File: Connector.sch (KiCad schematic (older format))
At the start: 1 part, among them J1 776163-1

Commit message: Added IO Lables
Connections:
- net labels added: +5VD, Accelerator_1, Accelerator_2, Brake_1, Brake_2, CAN_H, CAN_L, EmergencyStop, GND, GNDD, GearDrive, GearParking, GearReverse, HALL_1_+, HALL_1_-, HALL_2_+, HALL_2_-, HALL_3_+, HALL_3_-, HighVoltageOn, IgnitionOn, LeftSupport, NTC_AW_1, NTC_AW_2, NTC_FW_1, NTC_FW_2, ParkingBrake, PowerContactorOn, PowerSteeringPWM, ReverseLight, RightSupport, ShuntContactorOn, VIN
- net labels removed: +BATT, -BATT
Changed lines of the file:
@@
 $EndComp
 $Comp
-L power:+BATT #PWR?
-U 1 1 60F698CF
-P 3000 2400
-F 0 "#PWR?" H 3000 2250 50  0001 C CNN
-F 1 "+BATT" V 3015 2528 50  0000 L CNN
-F 2 "" H 3000 2400 50  0001 C CNN
-F 3 "" H 3000 2400 50  0001 C CNN
-	1    3000 2400
+L MyLibrary:VIN #PWR?
+U 1 1 610918C9
+P 3500 2150
+F 0 "#PWR?" H 3500 2000 50  0001 C CNN
+F 1 "VIN" V 3515 2278 50  0000 L CNN
+F 2 "" H 3500 2150 50  0001 C CNN
+F 3 "" H 3500 2150 50  0001 C CNN
+	1    3500 2150
 	0    1    1    0
 $EndComp
 $Comp
-L power:-BATT #PWR?
-U 1 1 60F6A98D
-P 3000 2550
-F 0 "#PWR?" H 3000 2400 50  0001 C CNN
-F 1 "-BATT" V 3015 2678 50  0000 L CNN
-F 2 "" H 3000 2550 50  0001 C CNN
-F 3 "" H 3000 2550 50  0001 C CNN
-	1    3000 2550
+L power:GND #PWR?
+U 1 1 61091F33
+P 3500 2250
+F 0 "#PWR?" H 3500 2000 50  0001 C CNN
+F 1 "GND" V 3505 2122 50  0000 R CNN
+F 2 "" H 3500 2250 50  0001 C CNN
+F 3 "" H 3500 2250 50  0001 C CNN
+	1    3500 2250
+	0    -1   -1   0
+$EndComp
+Text Label 3500 2500 0    50   ~ 0
+HALL_1_+
+Text Label 3500 2600 0    50   ~ 0
+HALL_1_-
+Text Label 3500 2700 0    50   ~ 0
+HALL_2_+
+Text Label 3500 2800 0    50   ~ 0
+HALL_2_-
+Text Label 3500 2900 0    50   ~ 0
+HALL_3_+
+Text Label 3500 3000 0    50   ~ 0
+HALL_3_-
+$Comp
+L power:+5VD #PWR?
+U 1 1 61093076
+P 3500 3100
+F 0 "#PWR?" H 3500 2950 50  0001 C CNN
+F 1 "+5VD" V 3515 3228 50  0000 L CNN
+F 2 "" H 3500 3100 50  0001 C CNN
+F 3 "" H 3500 3100 50  0001 C CNN
+	1    3500 3100
 	0    1    1    0
 $EndComp
+$Comp
+L power:GNDD #PWR?
+U 1 1 61093201
+P 3500 3200
+F 0 "#PWR?" H 3500 2950 50  0001 C CNN
+F 1 "GNDD" V 3504 3090 50  0000 R CNN
+F 2 "" H 3500 3200 50  0001 C CNN
+F 3 "" H 3500 3200 50  0001 C CNN
+	1    3500 3200
+	0    -1   -1   0
+$EndComp
+Text Label 3500 3350 0    50   ~ 0
+NTC_FW_1
+Text Label 3500 3450 0    50   ~ 0
+NTC_FW_2
+Text Label 3500 3550 0    50   ~ 0
+NTC_AW_1
+Text Label 3500 3650 0    50   ~ 0
+NTC_AW_2
+Text Label 3500 3850 0    50   ~ 0
+CAN_H
+Text Label 3500 3950 0    50   ~ 0
+CAN_L
+Text Label 3500 4200 0    50   ~ 0
+RightSupport
+Text Label 3500 4300 0    50   ~ 0
+LeftSupport
+Text Label 3500 4400 0    50   ~ 0
+IgnitionOn
+Text Label 3500 4500 0    50   ~ 0
+HighVoltageOn
+Text Label 3500 4600 0    50   ~ 0
+GearDrive
+Text Label 3500 4700 0    50   ~ 0
+GearReverse
+Text Label 3500 4800 0    50   ~ 0
+GearParking
+Text Label 3500 4900 0    50   ~ 0
+EmergencyStop
+Text Label 3500 5150 0    50   ~ 0
+ReverseLight
+Text Label 3500 5250 0    50   ~ 0
+ParkingBrake
+Text Label 3500 5350 0    50   ~ 0
+PowerContactorOn
+Text Label 3500 5450 0    50   ~ 0
+ShuntContactorOn
+Text Label 3500 5550 0    50   ~ 0
+PowerSteeringPWM
+Text Label 3500 5850 0    50   ~ 0
+Accelerator_1
+Text Label 3500 5950 0    50   ~ 0
+Accelerator_2
+Text Label 3500 6050 0    50   ~ 0
+Brake_1
+Text Label 3500 6150 0    50   ~ 0
+Brake_2
 $EndSCHEMATC

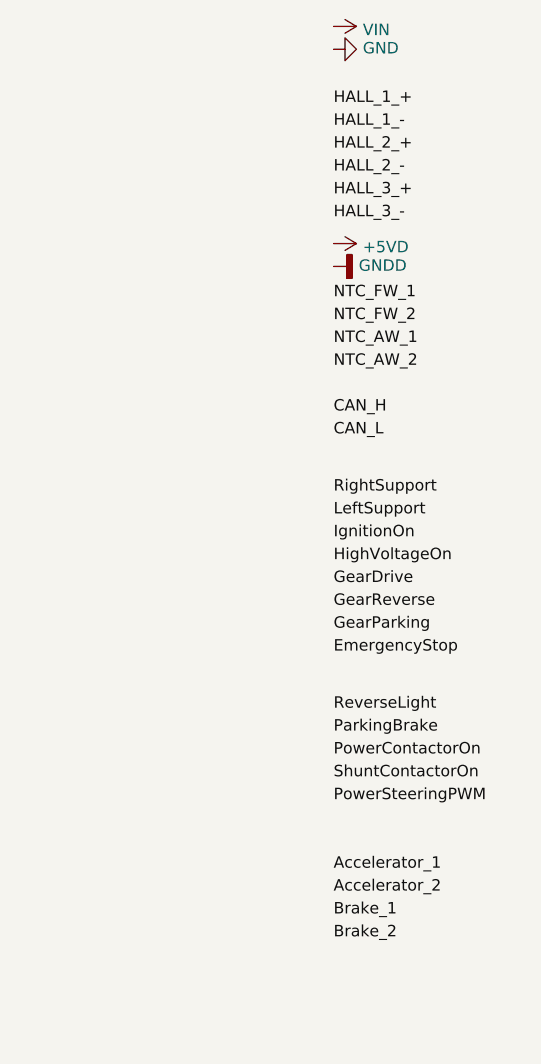
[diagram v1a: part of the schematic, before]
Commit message: Lables revised
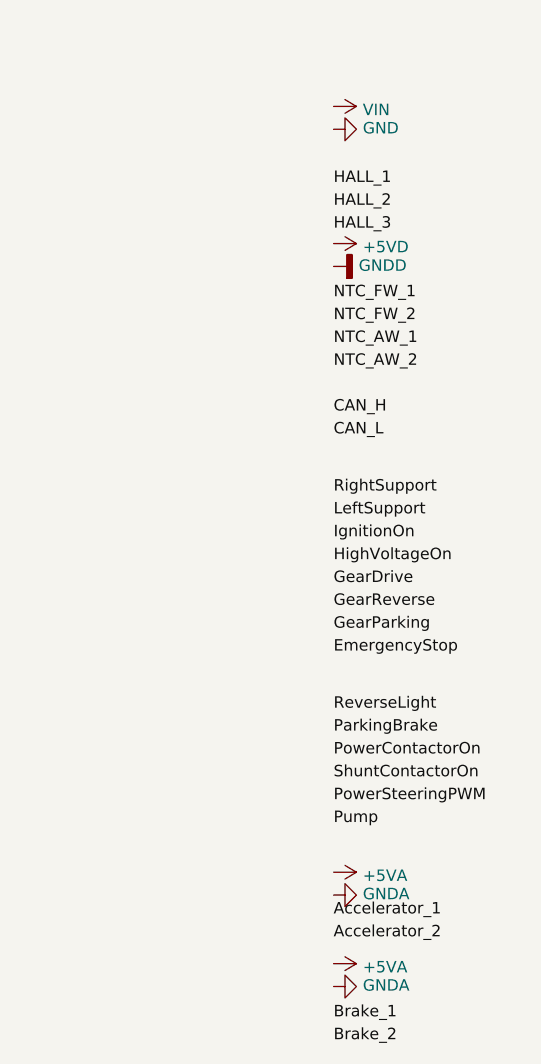
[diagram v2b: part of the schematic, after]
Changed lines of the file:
@@
 L MyLibrary:VIN #PWR?
 U 1 1 610918C9
-P 3500 2150
-F 0 "#PWR?" H 3500 2000 50  0001 C CNN
-F 1 "VIN" V 3515 2278 50  0000 L CNN
-F 2 "" H 3500 2150 50  0001 C CNN
-F 3 "" H 3500 2150 50  0001 C CNN
-	1    3500 2150
+P 3500 2500
+F 0 "#PWR?" H 3500 2350 50  0001 C CNN
+F 1 "VIN" V 3515 2628 50  0000 L CNN
+F 2 "" H 3500 2500 50  0001 C CNN
+F 3 "" H 3500 2500 50  0001 C CNN
+	1    3500 2500
 	0    1    1    0
 $EndComp
@@
 L power:GND #PWR?
 U 1 1 61091F33
-P 3500 2250
-F 0 "#PWR?" H 3500 2000 50  0001 C CNN
-F 1 "GND" V 3505 2122 50  0000 R CNN
-F 2 "" H 3500 2250 50  0001 C CNN
-F 3 "" H 3500 2250 50  0001 C CNN
-	1    3500 2250
+P 3500 2600
+F 0 "#PWR?" H 3500 2350 50  0001 C CNN
+F 1 "GND" V 3505 2472 50  0000 R CNN
+F 2 "" H 3500 2600 50  0001 C CNN
+F 3 "" H 3500 2600 50  0001 C CNN
+	1    3500 2600
 	0    -1   -1   0
 $EndComp
-Text Label 3500 2500 0    50   ~ 0
-HALL_1_+
-Text Label 3500 2600 0    50   ~ 0
-HALL_1_-
-Text Label 3500 2700 0    50   ~ 0
-HALL_2_+
-Text Label 3500 2800 0    50   ~ 0
-HALL_2_-
-Text Label 3500 2900 0    50   ~ 0
-HALL_3_+
-Text Label 3500 3000 0    50   ~ 0
-HALL_3_-
+Text Label 3500 2850 0    50   ~ 0
+HALL_1
+Text Label 3500 2950 0    50   ~ 0
+HALL_2
+Text Label 3500 3050 0    50   ~ 0
+HALL_3
 $Comp
 L power:+5VD #PWR?
@@
 Text Label 3500 5550 0    50   ~ 0
 PowerSteeringPWM
-Text Label 3500 5850 0    50   ~ 0
+Text Label 3500 6050 0    50   ~ 0
 Accelerator_1
-Text Label 3500 5950 0    50   ~ 0
+Text Label 3500 6150 0    50   ~ 0
 Accelerator_2
-Text Label 3500 6050 0    50   ~ 0
+Text Label 3500 6500 0    50   ~ 0
 Brake_1
-Text Label 3500 6150 0    50   ~ 0
+Text Label 3500 6600 0    50   ~ 0
 Brake_2
+Text Label 3500 5650 0    50   ~ 0
+Pump
+$Comp
+L power:+5VA #PWR?
+U 1 1 610A5DA3
+P 3500 5850
+F 0 "#PWR?" H 3500 5700 50  0001 C CNN
+F 1 "+5VA" V 3515 5978 50  0000 L CNN
+F 2 "" H 3500 5850 50  0001 C CNN
+F 3 "" H 3500 5850 50  0001 C CNN
+	1    3500 5850
+	0    1    1    0
+$EndComp
+$Comp
+L power:GNDA #PWR?
+U 1 1 610A5FEA
+P 3500 5950
+F 0 "#PWR?" H 3500 5700 50  0001 C CNN
+F 1 "GNDA" V 3505 5822 50  0000 R CNN
+F 2 "" H 3500 5950 50  0001 C CNN
+F 3 "" H 3500 5950 50  0001 C CNN
+	1    3500 5950
+	0    -1   -1   0
+$EndComp
+$Comp
+L power:+5VA #PWR?
+U 1 1 610A6A89
+P 3500 6250
+F 0 "#PWR?" H 3500 6100 50  0001 C CNN
+F 1 "+5VA" V 3515 6378 50  0000 L CNN
+F 2 "" H 3500 6250 50  0001 C CNN
+F 3 "" H 3500 6250 50  0001 C CNN
+	1    3500 6250
+	0    1    1    0
+$EndComp
+$Comp
+L power:GNDA #PWR?
+U 1 1 610A6A8F
+P 3500 6350
+F 0 "#PWR?" H 3500 6100 50  0001 C CNN
+F 1 "GNDA" V 3505 6222 50  0000 R CNN
+F 2 "" H 3500 6350 50  0001 C CNN
+F 3 "" H 3500 6350 50  0001 C CNN
+	1    3500 6350
+	0    -1   -1   0
+$EndComp
 $EndSCHEMATC

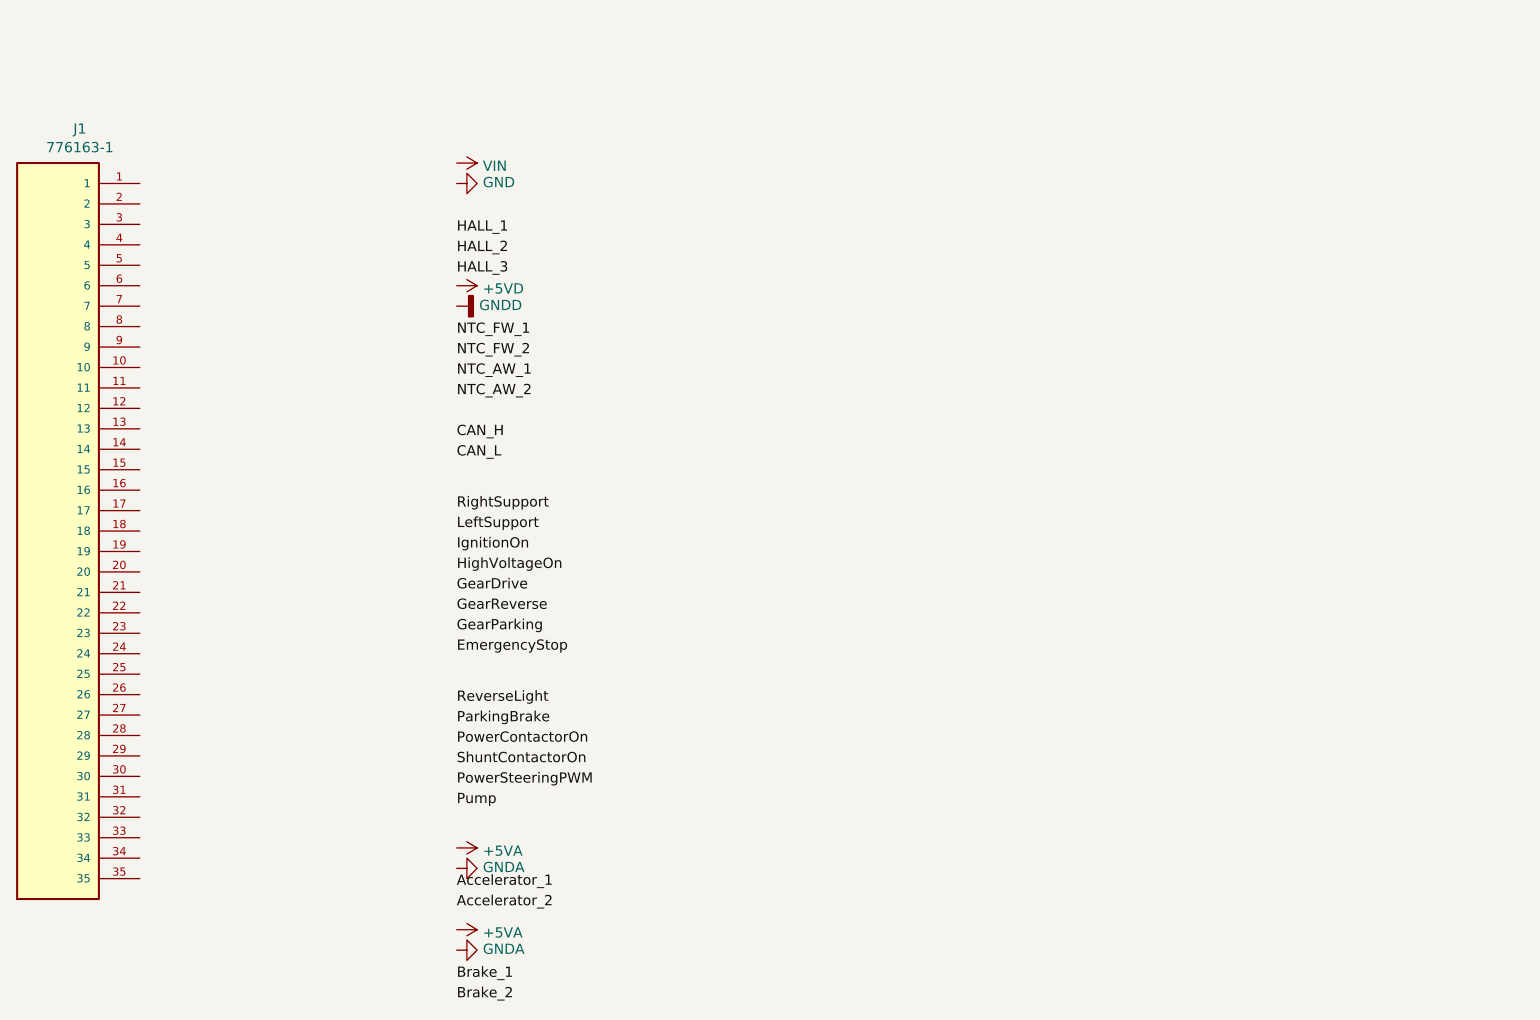
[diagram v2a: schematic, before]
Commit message: Added PCB Outline
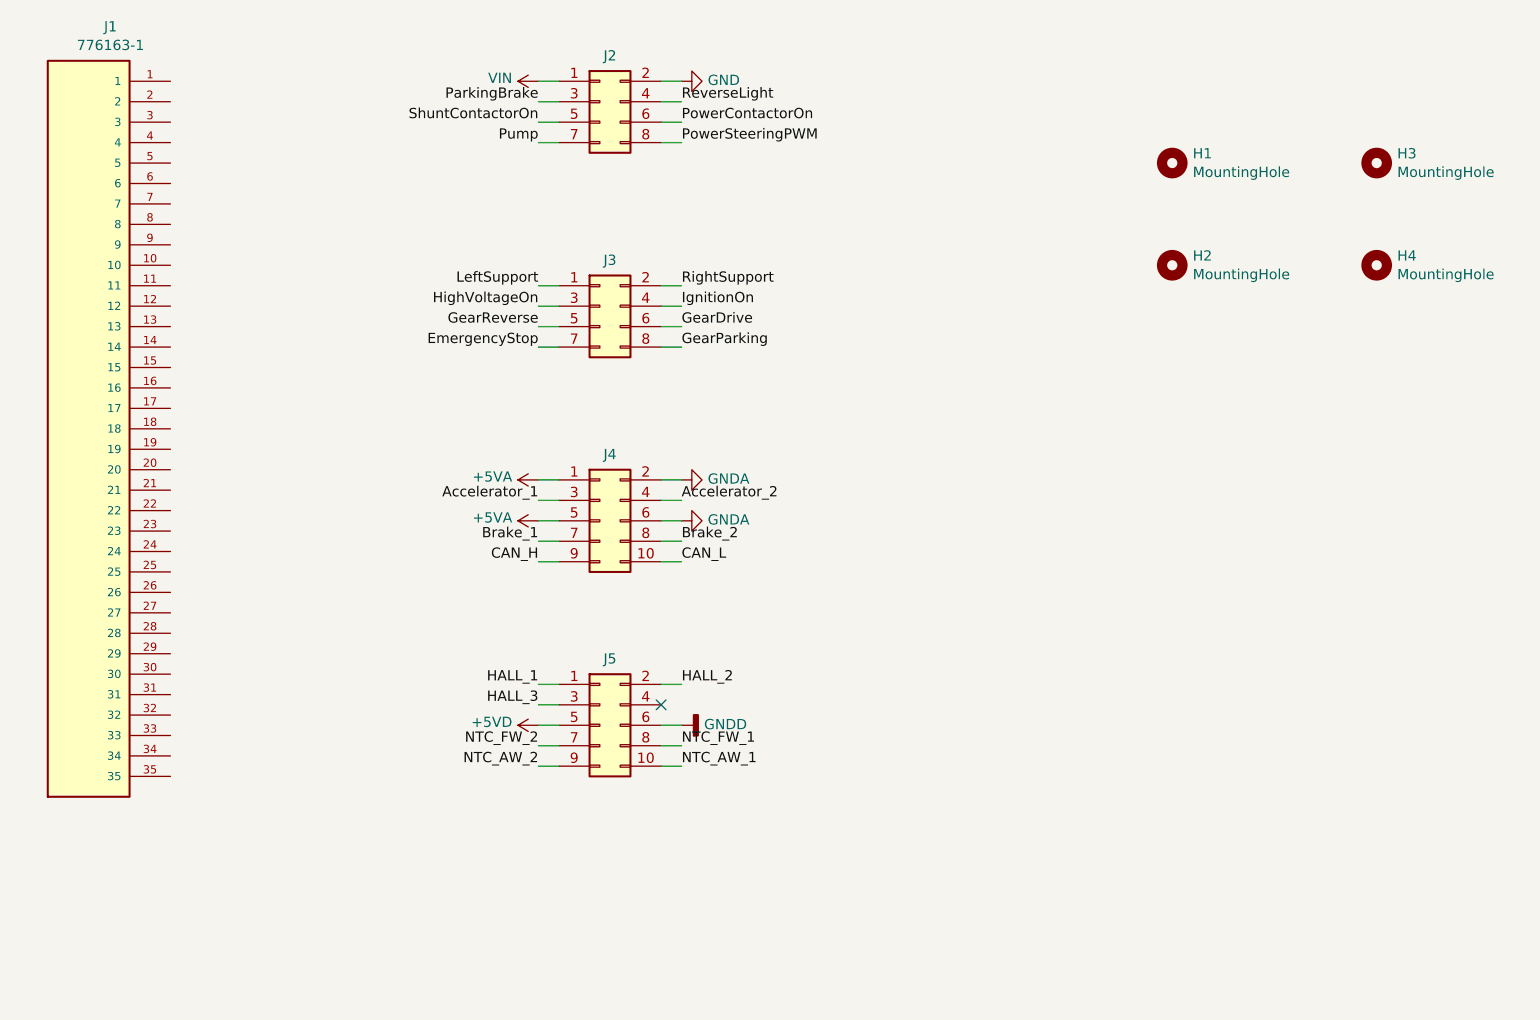
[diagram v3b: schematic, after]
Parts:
- added H1, H2, H3, H4: MountingHole, MountingHole:MountingHole_4.5mm, symbol Mechanical:MountingHole
- added J2, J3: Conn_02x04_Odd_Even, MyLibrary:Molex_Micro-Fit_3.0_43045-0800_2x04_P3.00mm_Horizontal, symbol Connector_Generic:Conn_02x04_Odd_Even
- added J4, J5: Conn_02x05_Odd_Even, MyLibrary:Molex_Micro-Fit_3.0_43045-1000_2x05_P3.00mm_Horizontal, symbol Connector_Generic:Conn_02x05_Odd_Even
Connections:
- net +5VA: now also J4.1 (Pin_1), J4.5 (Pin_5)
- net +5VD: now also J5.5 (Pin_5)
- net Accelerator_1: now also J4.3 (Pin_3)
- net Accelerator_2: now also J4.4 (Pin_4)
- net Brake_1: now also J4.7 (Pin_7)
- net Brake_2: now also J4.8 (Pin_8)
- net CAN_H: now also J4.9 (Pin_9)
- net CAN_L: now also J4.10 (Pin_10)
- net EmergencyStop: now also J3.7 (Pin_7)
- net GND: now also J2.2 (Pin_2)
- net GNDA: now also J4.2 (Pin_2), J4.6 (Pin_6)
- net GNDD: now also J5.6 (Pin_6)
- net GearDrive: now also J3.6 (Pin_6)
- net GearParking: now also J3.8 (Pin_8)
- net GearReverse: now also J3.5 (Pin_5)
- net HALL_1: now also J5.1 (Pin_1)
- net HALL_2: now also J5.2 (Pin_2)
- net HALL_3: now also J5.3 (Pin_3)
- net HighVoltageOn: now also J3.3 (Pin_3)
- net IgnitionOn: now also J3.4 (Pin_4)
- net LeftSupport: now also J3.1 (Pin_1)
- net NTC_AW_1: now also J5.10 (Pin_10)
- net NTC_AW_2: now also J5.9 (Pin_9)
- net NTC_FW_1: now also J5.8 (Pin_8)
- net NTC_FW_2: now also J5.7 (Pin_7)
- net ParkingBrake: now also J2.3 (Pin_3)
- net PowerContactorOn: now also J2.6 (Pin_6)
- net PowerSteeringPWM: now also J2.8 (Pin_8)
- net Pump: now also J2.7 (Pin_7)
- net ReverseLight: now also J2.4 (Pin_4)
- net RightSupport: now also J3.2 (Pin_2)
- net ShuntContactorOn: now also J2.5 (Pin_5)
- net VDD: now also J2.1 (Pin_1)
- no-connect marks 0 -> 1
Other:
- moved on the sheet: J1

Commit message: Added Connector PinOut and PCB layout
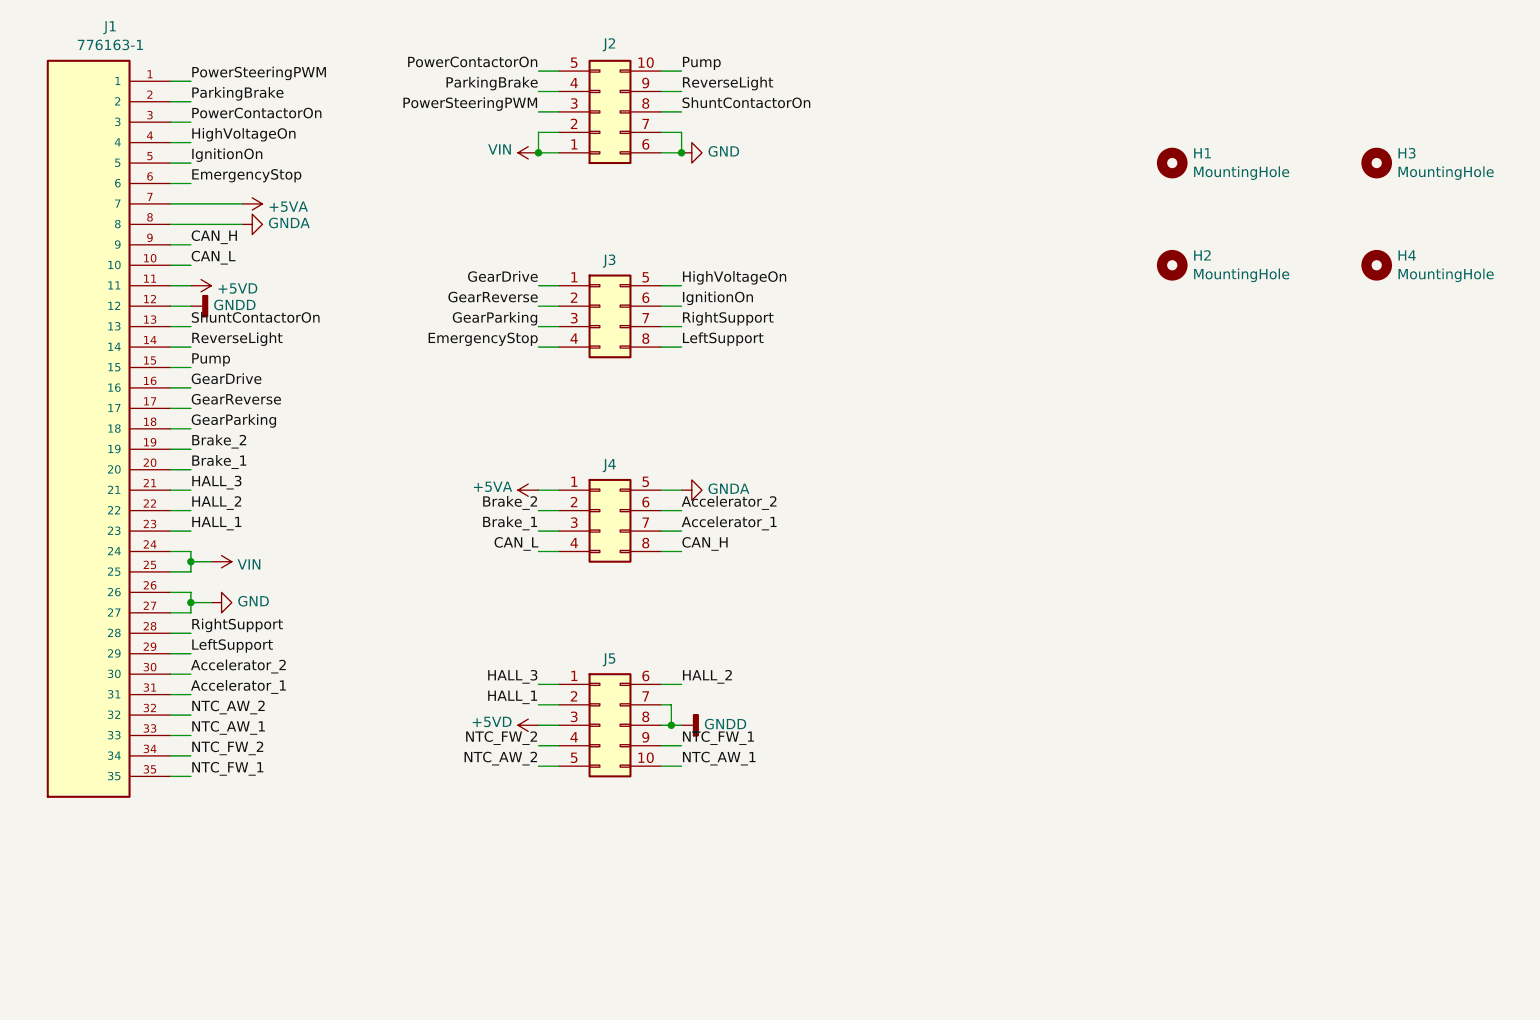
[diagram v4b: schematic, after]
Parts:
- removed J2, J3: Conn_02x04_Odd_Even, MyLibrary:Molex_Micro-Fit_3.0_43045-0800_2x04_P3.00mm_Horizontal, symbol Connector_Generic:Conn_02x04_Odd_Even
- removed J4, J5: Conn_02x05_Odd_Even, MyLibrary:Molex_Micro-Fit_3.0_43045-1000_2x05_P3.00mm_Horizontal, symbol Connector_Generic:Conn_02x05_Odd_Even
- added J2, J5: Conn_02x05_Top_Bottom, MyLibrary:Molex_Micro-Fit_3.0_43045-1000_2x05_P3.00mm_Horizontal, symbol Connector_Generic:Conn_02x05_Top_Bottom
- added J3, J4: Conn_02x04_Top_Bottom, MyLibrary:Molex_Micro-Fit_3.0_43045-0800_2x04_P3.00mm_Horizontal, symbol Connector_Generic:Conn_02x04_Top_Bottom
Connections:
- net +5VA: now also J1.7, J4.1 (Pin_1)
- net +5VD: now also J1.11, J5.3 (Pin_3)
- net Accelerator_1: now also J1.31, J4.7 (Pin_7)
- net Accelerator_2: now also J1.30, J4.6 (Pin_6)
- net Brake_1: now also J1.20, J4.3 (Pin_3)
- net Brake_2: now also J1.19, J4.2 (Pin_2)
- net CAN_H: now also J1.9, J4.8 (Pin_8)
- net CAN_L: now also J1.10, J4.4 (Pin_4)
- net EmergencyStop: now also J1.6, J3.4 (Pin_4)
- net GND: now also J1.26, J1.27, J2.6 (Pin_6), J2.7 (Pin_7)
- net GNDA: now also J1.8, J4.5 (Pin_5)
- net GNDD: now also J1.12, J5.7 (Pin_7), J5.8 (Pin_8)
- net GearDrive: now also J1.16, J3.1 (Pin_1)
- net GearParking: now also J1.18, J3.3 (Pin_3)
- net GearReverse: now also J1.17, J3.2 (Pin_2)
- net HALL_1: now also J1.23, J5.2 (Pin_2)
- net HALL_2: now also J1.22, J5.6 (Pin_6)
- net HALL_3: now also J1.21, J5.1 (Pin_1)
- net HighVoltageOn: now also J1.4, J3.5 (Pin_5)
- net IgnitionOn: now also J1.5, J3.6 (Pin_6)
- net LeftSupport: now also J1.29, J3.8 (Pin_8)
- net NTC_AW_1: now also J1.33, J5.10 (Pin_10)
- net NTC_AW_2: now also J1.32, J5.5 (Pin_5)
- net NTC_FW_1: now also J1.35, J5.9 (Pin_9)
- net NTC_FW_2: now also J1.34, J5.4 (Pin_4)
- net ParkingBrake: now also J1.2, J2.4 (Pin_4)
- net PowerContactorOn: now also J1.3, J2.5 (Pin_5)
- net PowerSteeringPWM: now also J1.1, J2.3 (Pin_3)
- net Pump: now also J1.15, J2.10 (Pin_10)
- net ReverseLight: now also J1.14, J2.9 (Pin_9)
- net RightSupport: now also J1.28, J3.7 (Pin_7)
- net ShuntContactorOn: now also J1.13, J2.8 (Pin_8)
- net VDD: now also J1.24, J1.25, J2.1 (Pin_1), J2.2 (Pin_2)
- no-connect marks 1 -> 0
